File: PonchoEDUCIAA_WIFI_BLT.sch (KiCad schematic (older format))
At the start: 3 parts

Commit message: Modificamos estructura de directorios
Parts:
- U?: footprint ESP32-footprints-Lib:ESP32-WROOM -> PonchoEDUCIAA_WIFI_BLT:ESP32-WROOM
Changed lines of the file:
@@
 LIBS:adc-dac
 LIBS:interface
+LIBS:ej2cese
 LIBS:PonchoEDUCIAA_WIFI_BLT
-LIBS:ej2cese
 LIBS:PonchoEDUCIAA_WIFI_BLT-cache
 EELAYER 25 0
@@
 F 0 "U?" H 5300 5300 60  0000 C CNN
 F 1 "ESP32-WROOM" H 6500 5300 60  0000 C CNN
-F 2 "ESP32-footprints-Lib:ESP32-WROOM" H 6350 5400 60  0001 C CNN
+F 2 "PonchoEDUCIAA_WIFI_BLT:ESP32-WROOM" H 6350 5400 60  0001 C CNN
 F 3 "" H 5550 4500 60  0001 C CNN
 	1    6000 4050

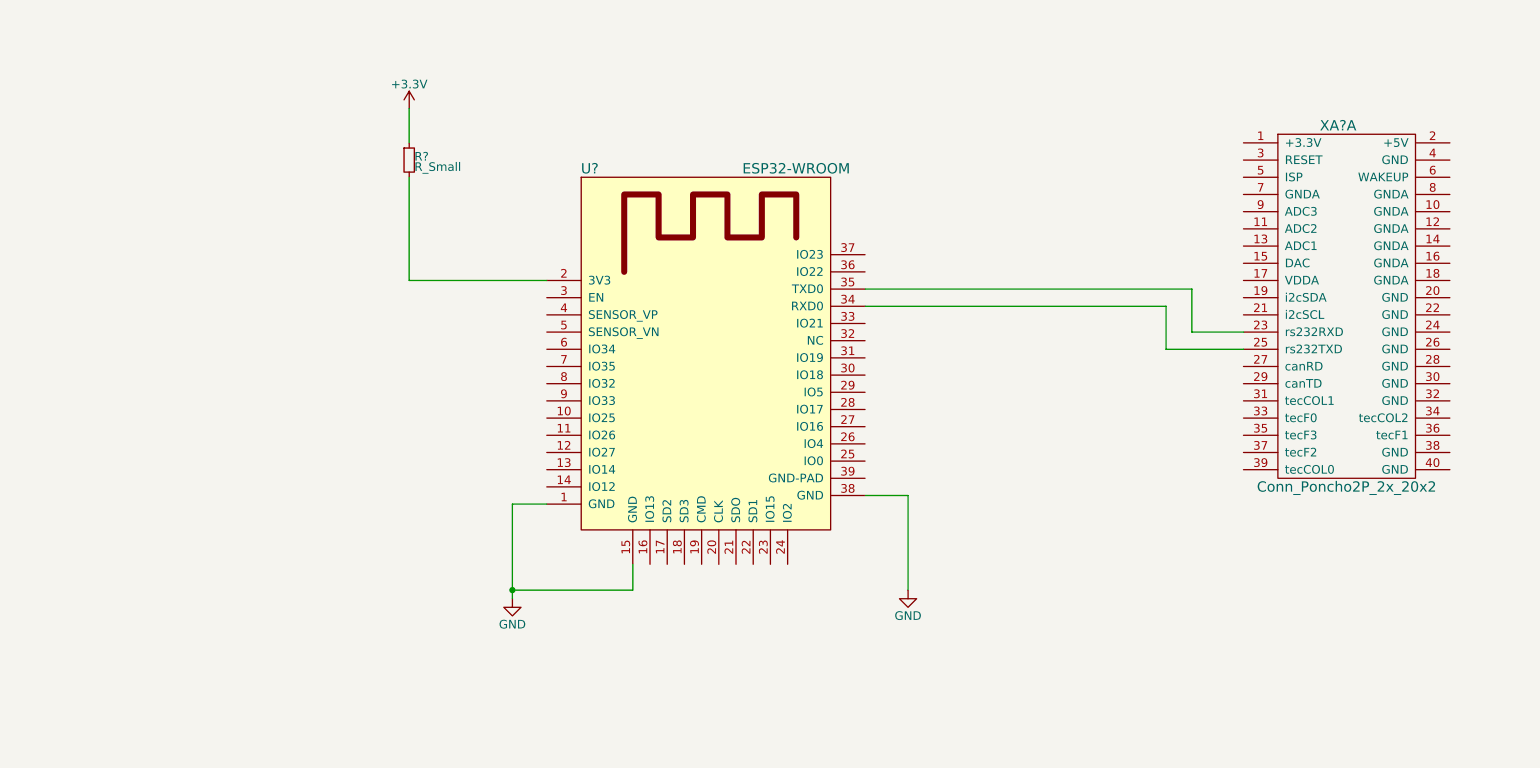
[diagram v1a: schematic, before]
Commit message: Agregamos leds al esquematico para la alimentación y la comunicación UART
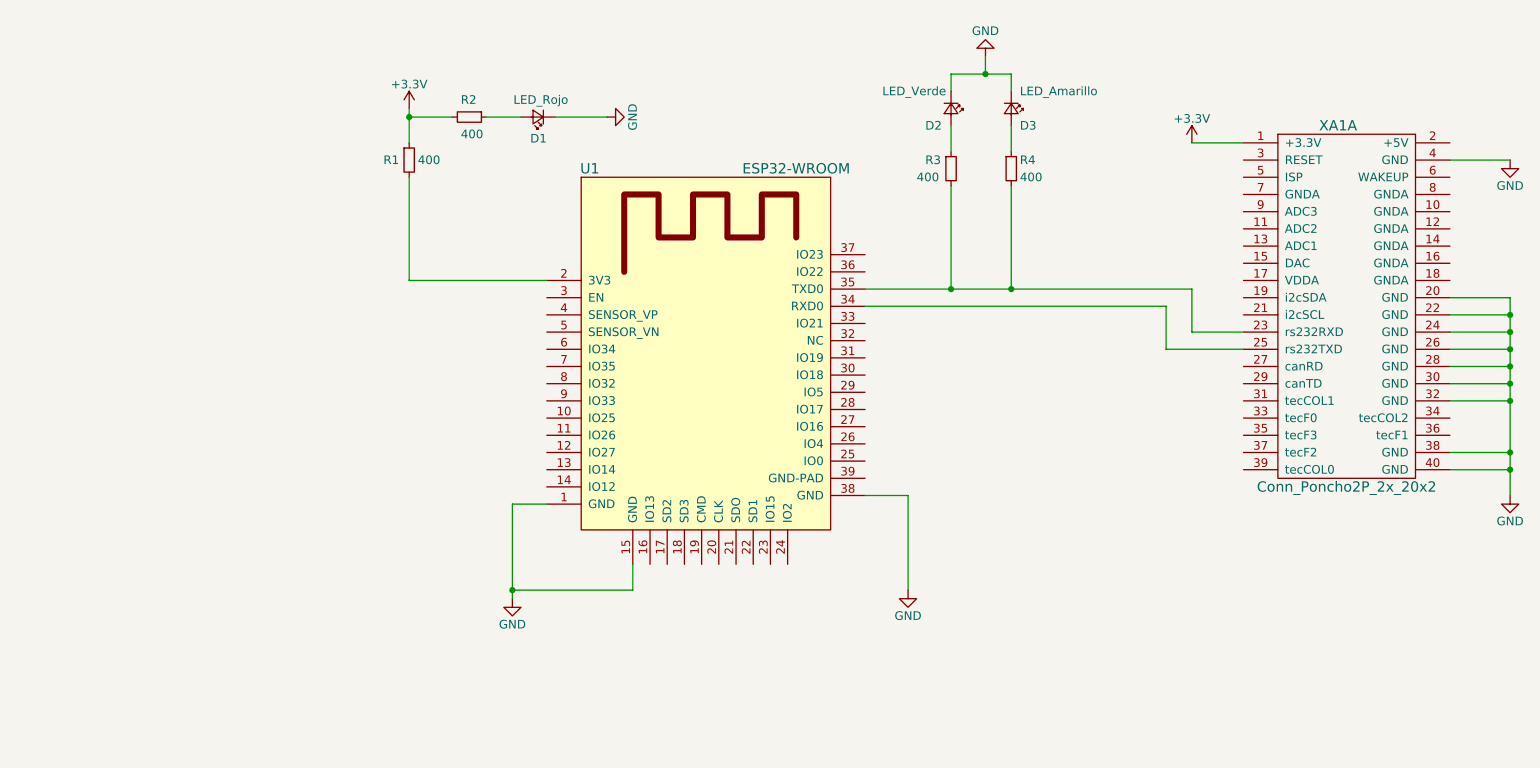
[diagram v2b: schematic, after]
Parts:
- added D1: LED_Rojo, symbol LED_Small
- added D2: LED_Verde, symbol LED_Small
- added D3: LED_Amarillo, symbol LED_Small
- added R2, R3, R4: 400, symbol R_Small
- R1: renamed from R?; value R_Small -> 400
- gave numbers to parts that had none: 2
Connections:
- net +3V3: now also XA1.1 (+3.3V), R2.2
- net GND: now also XA1.20 (GND), XA1.22 (GND), XA1.24 (GND), XA1.26 (GND), XA1.28 (GND), XA1.30 (GND), XA1.32 (GND), XA1.38 (GND), XA1.4 (GND), XA1.40 (GND), D1.1 (K), D2.1 (K), D3.1 (K)
- net at U1.35 (TXD0), XA1.23 (rs232RXD): now also R3.2, R4.2
- new net: D2.2 (A), R3.1
- new net: D3.2 (A), R4.1
- new net: D1.2 (A), R2.1
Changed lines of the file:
@@
 encoding utf-8
 Sheet 1 1
-Title ""
+Title "Poncho EDU-CIAA WIFI-BLUETOOTH"
 Date ""
-Rev ""
+Rev "1.0"
 Comp ""
-Comment1 ""
-Comment2 ""
+Comment1 "Licencia BSD"
+Comment2 "Autor: Julio Gastón Coccé"
 Comment3 ""
 Comment4 ""
 $EndDescr
 $Comp
-L ESP32-WROOM U?
+L ESP32-WROOM U1
 U 1 1 5911A5F3
 P 6000 4050
-F 0 "U?" H 5300 5300 60  0000 C CNN
+F 0 "U1" H 5300 5300 60  0000 C CNN
 F 1 "ESP32-WROOM" H 6500 5300 60  0000 C CNN
 F 2 "PonchoEDUCIAA_WIFI_BLT:ESP32-WROOM" H 6350 5400 60  0001 C CNN
@@
 	7150 4700 7150 5250
 $Comp
-L Conn_Poncho2P_2x_20x2 XA?
+L Conn_Poncho2P_2x_20x2 XA1
 U 1 1 5911AAD2
 P 9350 2950
-F 0 "XA?" H 9650 3350 60  0000 C CNN
+F 0 "XA1" H 9650 3350 60  0000 C CNN
 F 1 "Conn_Poncho2P_2x_20x2" H 9700 1250 60  0000 C CNN
 F 2 "" H 9350 2950 60  0000 C CNN
@@
 	8800 3750 9100 3750
 $Comp
-L R_Small R?
+L R_Small R1
 U 1 1 5911BB36
 P 4250 2750
-F 0 "R?" H 4280 2770 50  0000 L CNN
-F 1 "R_Small" H 4280 2710 50  0000 L CNN
+F 0 "R1" H 4100 2750 50  0000 L CNN
+F 1 "400" H 4300 2750 50  0000 L CNN
 F 2 "" H 4250 2750 50  0001 C CNN
 F 3 "" H 4250 2750 50  0001 C CNN
@@
 Wire Wire Line
 	4250 2450 4250 2650
+$Comp
+L R_Small R3
+U 1 1 5915BEE9
+P 7400 2800
+F 0 "R3" H 7250 2850 50  0000 L CNN
+F 1 "400" H 7200 2750 50  0000 L CNN
+F 2 "" H 7400 2800 50  0001 C CNN
+F 3 "" H 7400 2800 50  0001 C CNN
+	1    7400 2800
+	1    0    0    -1
+$EndComp
+$Comp
+L GND #PWR?
+U 1 1 5915C0A7
+P 7600 2150
+F 0 "#PWR?" H 7600 1900 50  0001 C CNN
+F 1 "GND" H 7600 2000 50  0000 C CNN
+F 2 "" H 7600 2150 50  0001 C CNN
+F 3 "" H 7600 2150 50  0001 C CNN
+	1    7600 2150
+	-1   0    0    1
+$EndComp
+$Comp
+L LED_Small D2
+U 1 1 5915C18C
+P 7400 2450
+F 0 "D2" V 7500 2300 50  0000 L CNN
+F 1 "LED_Verde" V 7300 2050 50  0000 L CNN
+F 2 "" V 7400 2450 50  0001 C CNN
+F 3 "" V 7400 2450 50  0001 C CNN
+	1    7400 2450
+	0    1    1    0
+$EndComp
+Wire Wire Line
+	7400 2700 7400 2550
+Wire Wire Line
+	7400 2900 7400 3500
+Connection ~ 7400 3500
+$Comp
+L R_Small R4
+U 1 1 5915C27A
+P 7750 2800
+F 0 "R4" H 7800 2850 50  0000 L CNN
+F 1 "400" H 7800 2750 50  0000 L CNN
+F 2 "" H 7750 2800 50  0001 C CNN
+F 3 "" H 7750 2800 50  0001 C CNN
+	1    7750 2800
+	1    0    0    -1
+$EndComp
+$Comp
+L LED_Small D3
+U 1 1 5915C2A8
+P 7750 2450
+F 0 "D3" V 7850 2500 50  0000 L CNN
+F 1 "LED_Amarillo" V 7650 2500 50  0000 L CNN
+F 2 "" V 7750 2450 50  0001 C CNN
+F 3 "" V 7750 2450 50  0001 C CNN
+	1    7750 2450
+	0    1    1    0
+$EndComp
+Wire Wire Line
+	7750 2900 7750 3500
+Connection ~ 7750 3500
+Wire Wire Line
+	7750 2700 7750 2550
+Wire Wire Line
+	7400 2350 7400 2250
+Wire Wire Line
+	7400 2250 7750 2250
+Wire Wire Line
+	7600 2250 7600 2150
+Wire Wire Line
+	7750 2250 7750 2350
+Connection ~ 7600 2250
+$Comp
+L R_Small R2
+U 1 1 5915C673
+P 4600 2500
+F 0 "R2" V 4500 2450 50  0000 L CNN
+F 1 "400" V 4700 2450 50  0000 L CNN
+F 2 "" H 4600 2500 50  0001 C CNN
+F 3 "" H 4600 2500 50  0001 C CNN
+	1    4600 2500
+	0    1    1    0
+$EndComp
+$Comp
+L LED_Small D1
+U 1 1 5915C6BB
+P 5000 2500
+F 0 "D1" H 4950 2625 50  0000 L CNN
+F 1 "LED_Rojo" H 4825 2400 50  0000 L CNN
+F 2 "" V 5000 2500 50  0001 C CNN
+F 3 "" V 5000 2500 50  0001 C CNN
+	1    5000 2500
+	-1   0    0    1
+$EndComp
+$Comp
+L GND #PWR?
+U 1 1 5915C716
+P 5400 2500
+F 0 "#PWR?" H 5400 2250 50  0001 C CNN
+F 1 "GND" H 5400 2350 50  0000 C CNN
+F 2 "" H 5400 2500 50  0001 C CNN
+F 3 "" H 5400 2500 50  0001 C CNN
+	1    5400 2500
+	0    -1   -1   0
+$EndComp
+Wire Wire Line
+	4500 2500 4250 2500
+Connection ~ 4250 2500
+Wire Wire Line
+	4700 2500 4900 2500
+Wire Wire Line
+	5100 2500 5400 2500
+$Comp
+L +3.3V #PWR?
+U 1 1 5915E17D
+P 8800 2650
+F 0 "#PWR?" H 8800 2500 50  0001 C CNN
+F 1 "+3.3V" H 8800 2790 50  0000 C CNN
+F 2 "" H 8800 2650 50  0001 C CNN
+F 3 "" H 8800 2650 50  0001 C CNN
+	1    8800 2650
+	1    0    0    -1
+$EndComp
+Wire Wire Line
+	9100 2650 8800 2650
+$Comp
+L GND #PWR?
+U 1 1 5915E6C2
+P 10650 2750
+F 0 "#PWR?" H 10650 2500 50  0001 C CNN
+F 1 "GND" H 10650 2600 50  0000 C CNN
+F 2 "" H 10650 2750 50  0001 C CNN
+F 3 "" H 10650 2750 50  0001 C CNN
+	1    10650 2750
+	1    0    0    -1
+$EndComp
+Wire Wire Line
+	10300 2750 10650 2750
+$Comp
+L GND #PWR?
+U 1 1 5915ECBD
+P 10650 4700
+F 0 "#PWR?" H 10650 4450 50  0001 C CNN
+F 1 "GND" H 10650 4550 50  0000 C CNN
+F 2 "" H 10650 4700 50  0001 C CNN
+F 3 "" H 10650 4700 50  0001 C CNN
+	1    10650 4700
+	1    0    0    -1
+$EndComp
+Wire Wire Line
+	10300 3550 10650 3550
+Wire Wire Line
+	10650 3550 10650 4700
+Wire Wire Line
+	10300 3650 10650 3650
+Connection ~ 10650 3650
+Wire Wire Line
+	10300 3750 10650 3750
+Connection ~ 10650 3750
+Wire Wire Line
+	10300 3850 10650 3850
+Connection ~ 10650 3850
+Wire Wire Line
+	10300 3950 10650 3950
+Connection ~ 10650 3950
+Wire Wire Line
+	10300 4050 10650 4050
+Connection ~ 10650 4050
+Wire Wire Line
+	10300 4150 10650 4150
+Connection ~ 10650 4150
+Wire Wire Line
+	10300 4450 10650 4450
+Connection ~ 10650 4450
+Wire Wire Line
+	10300 4550 10650 4550
+Connection ~ 10650 4550
 $EndSCHEMATC

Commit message: Agregado de circuitos al esquematico
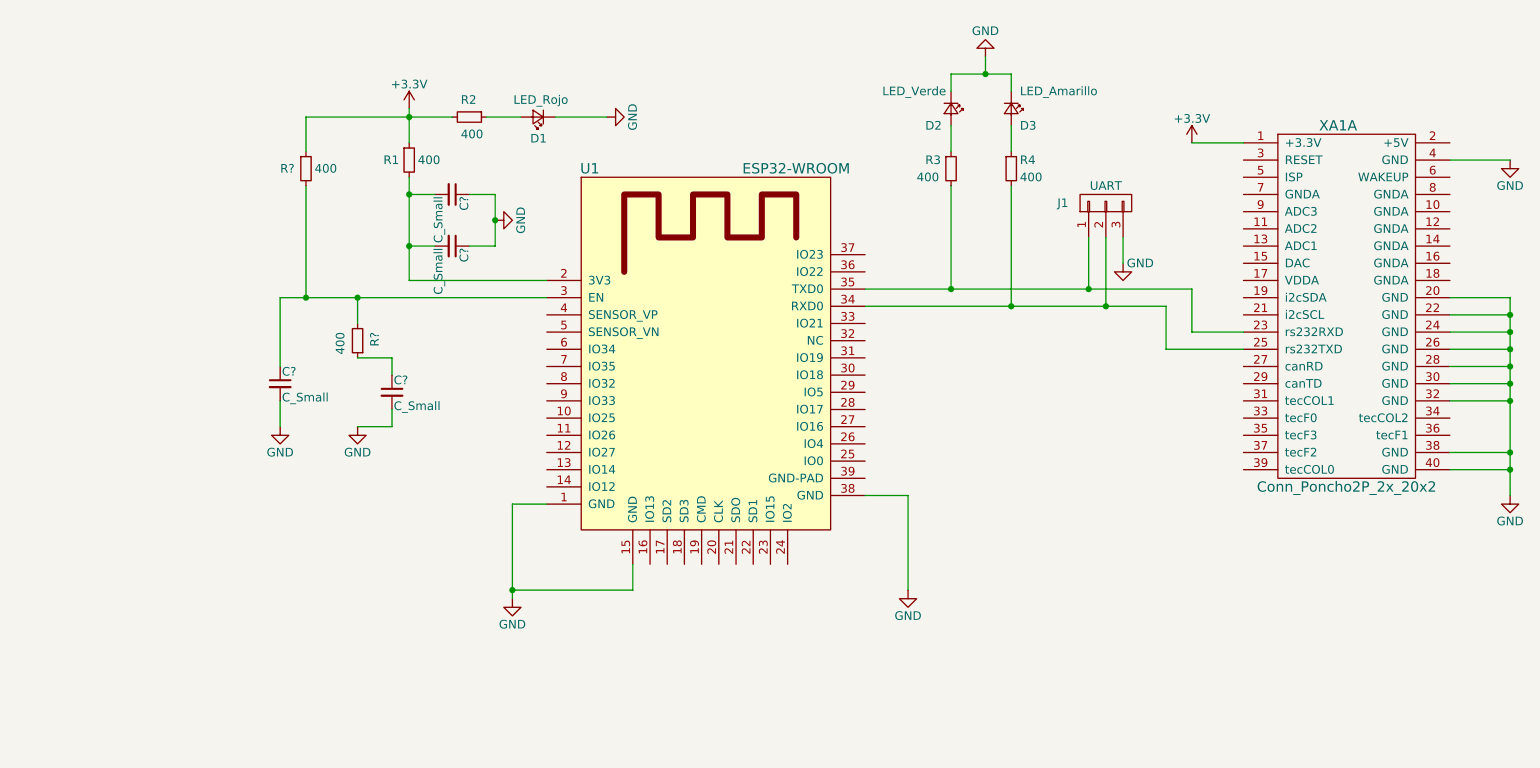
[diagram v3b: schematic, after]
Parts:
- added C? (x4): C_Small, symbol C_Small
- added J1: UART, symbol CONN_01X03
- added R? (x2): 400, symbol R_Small
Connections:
- net +3V3: now also R?.1
- net GND: now also C?.1, C?.1, C?.2, C?.2, J1.3 (P3)
- net at R1.2, U1.2 (3V3): now also C?.2, C?.2
- net at U1.3 (EN): now also C?.1, R?.2, R?.2
- net at U1.34 (RXD0), XA1.25 (rs232TXD): now also R4.2, J1.2 (P2)
- net at R3.2, U1.35 (TXD0), XA1.23 (rs232RXD): now also J1.1 (P1); no longer R4.2
- new net: C?.1, R?.1
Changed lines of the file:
@@
 $EndComp
-Wire Wire Line
-	7750 2900 7750 3500
-Connection ~ 7750 3500
 Wire Wire Line
 	7750 2700 7750 2550
@@
 $EndComp
 Wire Wire Line
-	4500 2500 4250 2500
+	3650 2500 4500 2500
 Connection ~ 4250 2500
 Wire Wire Line
@@
 	10300 4550 10650 4550
 Connection ~ 10650 4550
+Wire Wire Line
+	7750 2900 7750 3600
+Connection ~ 7750 3600
+$Comp
+L CONN_01X03 J1
+U 1 1 591B2551
+P 8300 3000
+F 0 "J1" V 8300 3250 50  0000 C CNN
+F 1 "UART" V 8400 3000 50  0000 C CNN
+F 2 "" H 8300 3000 50  0001 C CNN
+F 3 "" H 8300 3000 50  0001 C CNN
+	1    8300 3000
+	0    -1   -1   0
+$EndComp
+Wire Wire Line
+	8300 3200 8300 3600
+Connection ~ 8300 3600
+Wire Wire Line
+	8200 3200 8200 3500
+Connection ~ 8200 3500
+$Comp
+L GND #PWR?
+U 1 1 591B26D5
+P 8400 3350
+F 0 "#PWR?" H 8400 3100 50  0001 C CNN
+F 1 "GND" H 8500 3350 50  0000 C CNN
+F 2 "" H 8400 3350 50  0001 C CNN
+F 3 "" H 8400 3350 50  0001 C CNN
+	1    8400 3350
+	1    0    0    -1
+$EndComp
+Wire Wire Line
+	8400 3350 8400 3200
+$Comp
+L GND #PWR?
+U 1 1 591B2EEF
+P 3950 4300
+F 0 "#PWR?" H 3950 4050 50  0001 C CNN
+F 1 "GND" H 3950 4150 50  0000 C CNN
+F 2 "" H 3950 4300 50  0001 C CNN
+F 3 "" H 3950 4300 50  0001 C CNN
+	1    3950 4300
+	1    0    0    -1
+$EndComp
+$Comp
+L C_Small C?
+U 1 1 591B3654
+P 4150 4100
+F 0 "C?" H 4160 4170 50  0000 L CNN
+F 1 "C_Small" H 4160 4020 50  0000 L CNN
+F 2 "" H 4150 4100 50  0001 C CNN
+F 3 "" H 4150 4100 50  0001 C CNN
+	1    4150 4100
+	1    0    0    -1
+$EndComp
+$Comp
+L C_Small C?
+U 1 1 591B36A3
+P 4500 2950
+F 0 "C?" H 4510 3020 50  0000 L CNN
+F 1 "C_Small" H 4510 2870 50  0000 L CNN
+F 2 "" H 4500 2950 50  0001 C CNN
+F 3 "" H 4500 2950 50  0001 C CNN
+	1    4500 2950
+	0    1    1    0
+$EndComp
+$Comp
+L C_Small C?
+U 1 1 591B3730
+P 4500 3250
+F 0 "C?" H 4510 3320 50  0000 L CNN
+F 1 "C_Small" H 4510 3170 50  0000 L CNN
+F 2 "" H 4500 3250 50  0001 C CNN
+F 3 "" H 4500 3250 50  0001 C CNN
+	1    4500 3250
+	0    1    1    0
+$EndComp
+$Comp
+L GND #PWR?
+U 1 1 591B3773
+P 4750 3100
+F 0 "#PWR?" H 4750 2850 50  0001 C CNN
+F 1 "GND" H 4750 2950 50  0000 C CNN
+F 2 "" H 4750 3100 50  0001 C CNN
+F 3 "" H 4750 3100 50  0001 C CNN
+	1    4750 3100
+	0    -1   -1   0
+$EndComp
+Wire Wire Line
+	4600 2950 4750 2950
+Wire Wire Line
+	4750 2950 4750 3250
+Wire Wire Line
+	4750 3250 4600 3250
+Connection ~ 4750 3100
+Wire Wire Line
+	4400 2950 4250 2950
+Connection ~ 4250 2950
+Wire Wire Line
+	4400 3250 4250 3250
+Connection ~ 4250 3250
+Wire Wire Line
+	3500 3550 5050 3550
+$Comp
+L R_Small R?
+U 1 1 591B39FC
+P 3950 3800
+F 0 "R?" V 3850 3750 50  0000 L CNN
+F 1 "400" V 4050 3750 50  0000 L CNN
+F 2 "" H 3950 3800 50  0001 C CNN
+F 3 "" H 3950 3800 50  0001 C CNN
+	1    3950 3800
+	-1   0    0    1
+$EndComp
+Wire Wire Line
+	3950 3700 3950 3550
+Connection ~ 3950 3550
+Wire Wire Line
+	4150 4000 4150 3900
+Wire Wire Line
+	4150 3900 3950 3900
+Wire Wire Line
+	3950 4300 4150 4300
+Wire Wire Line
+	4150 4300 4150 4200
+$Comp
+L R_Small R?
+U 1 1 591B3C47
+P 3650 2800
+F 0 "R?" H 3500 2800 50  0000 L CNN
+F 1 "400" H 3700 2800 50  0000 L CNN
+F 2 "" H 3650 2800 50  0001 C CNN
+F 3 "" H 3650 2800 50  0001 C CNN
+	1    3650 2800
+	1    0    0    -1
+$EndComp
+Wire Wire Line
+	3650 2500 3650 2700
+Wire Wire Line
+	3650 3550 3650 2900
+$Comp
+L C_Small C?
+U 1 1 591B3D46
+P 3500 4050
+F 0 "C?" H 3510 4120 50  0000 L CNN
+F 1 "C_Small" H 3510 3970 50  0000 L CNN
+F 2 "" H 3500 4050 50  0001 C CNN
+F 3 "" H 3500 4050 50  0001 C CNN
+	1    3500 4050
+	1    0    0    -1
+$EndComp
+$Comp
+L GND #PWR?
+U 1 1 591B3D9C
+P 3500 4300
+F 0 "#PWR?" H 3500 4050 50  0001 C CNN
+F 1 "GND" H 3500 4150 50  0000 C CNN
+F 2 "" H 3500 4300 50  0001 C CNN
+F 3 "" H 3500 4300 50  0001 C CNN
+	1    3500 4300
+	1    0    0    -1
+$EndComp
+Wire Wire Line
+	3500 3550 3500 3950
+Connection ~ 3650 3550
+Wire Wire Line
+	3500 4150 3500 4300
 $EndSCHEMATC

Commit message: Ultimos agregados al esquematico
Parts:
- added C5: 1nF/10V, symbol C_Small
- added R7: 5k, symbol R_Small
- added R8: 470, symbol R_Small
- C1: renamed from C?; value C_Small -> 0,1uF/10V
- C2: renamed from C?; value C_Small -> 10uF/6,3V
- C3: renamed from C?; value C_Small -> 1nF/50V
- C4: renamed from C?; value C_Small -> 0,1nF/50V
- R5: renamed from R?; value 400 -> 10k
- R6: renamed from R?; value 400 -> 470
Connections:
- net +3V3: now also R7.1
- net GND: now also U1.24 (IO2), U1.39 (GND-PAD), C5.1
- net at U1.25 (IO0): now also R7.2, R8.2
- new net: C5.2, R8.1
- no-connect marks 0 -> 54
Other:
- moved on the sheet: C1, C2, C3, C4, D1, D2, D3, J1, R1, R2, R3, R4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
